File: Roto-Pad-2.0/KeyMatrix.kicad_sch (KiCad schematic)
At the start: 50 parts

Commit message: completed schematic, passes ERC
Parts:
- D1, D10, D11, D12, D13, D14, D15, D16, D17, D18, D19, D2, D20, D21, D22, D23, D24, D25, D3, D4, D5, D6, D7, D8, D9: footprint (none) -> PCM_Diode_SMD_AKL:D_1206_3216Metric_Castellated
- SW1: renamed from S1; value Key -> Switch; footprint (none) -> PCM_Switch_Keyboard_Hotswap_Kailh:SW_Hotswap_Kailh_MX_1.00u; symbol PCM_Elektuur:S-make -> Custom:MX_Keyswitch; Rating V/A -> (none)
- SW10: renamed from S10; value Key -> Switch; footprint (none) -> PCM_Switch_Keyboard_Hotswap_Kailh:SW_Hotswap_Kailh_MX_1.00u; symbol PCM_Elektuur:S-make -> Custom:MX_Keyswitch; Rating V/A -> (none)
- SW11: renamed from S11; value Key -> Switch; footprint (none) -> PCM_Switch_Keyboard_Hotswap_Kailh:SW_Hotswap_Kailh_MX_1.00u; symbol PCM_Elektuur:S-make -> Custom:MX_Keyswitch; Rating V/A -> (none)
- SW12: renamed from S12; value Key -> Switch; footprint (none) -> PCM_Switch_Keyboard_Hotswap_Kailh:SW_Hotswap_Kailh_MX_1.00u; symbol PCM_Elektuur:S-make -> Custom:MX_Keyswitch; Rating V/A -> (none)
- SW13: renamed from S13; value Key -> Switch; footprint (none) -> PCM_Switch_Keyboard_Hotswap_Kailh:SW_Hotswap_Kailh_MX_1.00u; symbol PCM_Elektuur:S-make -> Custom:MX_Keyswitch; Rating V/A -> (none)
- SW14: renamed from S14; value Key -> Switch; footprint (none) -> PCM_Switch_Keyboard_Hotswap_Kailh:SW_Hotswap_Kailh_MX_1.00u; symbol PCM_Elektuur:S-make -> Custom:MX_Keyswitch; Rating V/A -> (none)
- SW15: renamed from S15; value Key -> Switch; footprint (none) -> PCM_Switch_Keyboard_Hotswap_Kailh:SW_Hotswap_Kailh_MX_1.00u; symbol PCM_Elektuur:S-make -> Custom:MX_Keyswitch; Rating V/A -> (none)
- SW16: renamed from S16; value Key -> Switch; footprint (none) -> PCM_Switch_Keyboard_Hotswap_Kailh:SW_Hotswap_Kailh_MX_1.00u; symbol PCM_Elektuur:S-make -> Custom:MX_Keyswitch; Rating V/A -> (none)
- SW17: renamed from S17; value Key -> Switch; footprint (none) -> PCM_Switch_Keyboard_Hotswap_Kailh:SW_Hotswap_Kailh_MX_1.00u; symbol PCM_Elektuur:S-make -> Custom:MX_Keyswitch; Rating V/A -> (none)
- SW18: renamed from S18; value Key -> Switch; footprint (none) -> PCM_Switch_Keyboard_Hotswap_Kailh:SW_Hotswap_Kailh_MX_1.00u; symbol PCM_Elektuur:S-make -> Custom:MX_Keyswitch; Rating V/A -> (none)
- SW19: renamed from S19; value Key -> Switch; footprint (none) -> PCM_Switch_Keyboard_Hotswap_Kailh:SW_Hotswap_Kailh_MX_1.00u; symbol PCM_Elektuur:S-make -> Custom:MX_Keyswitch; Rating V/A -> (none)
- SW2: renamed from S2; value Key -> Switch; footprint (none) -> PCM_Switch_Keyboard_Hotswap_Kailh:SW_Hotswap_Kailh_MX_1.00u; symbol PCM_Elektuur:S-make -> Custom:MX_Keyswitch; Rating V/A -> (none)
- SW20: renamed from S20; value Key -> Switch; footprint (none) -> PCM_Switch_Keyboard_Hotswap_Kailh:SW_Hotswap_Kailh_MX_1.00u; symbol PCM_Elektuur:S-make -> Custom:MX_Keyswitch; Rating V/A -> (none)
- SW21: renamed from S21; value Key -> Switch; footprint (none) -> PCM_Switch_Keyboard_Hotswap_Kailh:SW_Hotswap_Kailh_MX_1.00u; symbol PCM_Elektuur:S-make -> Custom:MX_Keyswitch; Rating V/A -> (none)
- SW22: renamed from S22; value Key -> Switch; footprint (none) -> PCM_Switch_Keyboard_Hotswap_Kailh:SW_Hotswap_Kailh_MX_1.00u; symbol PCM_Elektuur:S-make -> Custom:MX_Keyswitch; Rating V/A -> (none)
- SW23: renamed from S23; value Key -> Switch; footprint (none) -> PCM_Switch_Keyboard_Hotswap_Kailh:SW_Hotswap_Kailh_MX_1.00u; symbol PCM_Elektuur:S-make -> Custom:MX_Keyswitch; Rating V/A -> (none)
- SW24: renamed from S24; value Key -> Switch; footprint (none) -> PCM_Switch_Keyboard_Hotswap_Kailh:SW_Hotswap_Kailh_MX_1.00u; symbol PCM_Elektuur:S-make -> Custom:MX_Keyswitch; Rating V/A -> (none)
- SW25: renamed from S25; value Key -> Switch; footprint (none) -> PCM_Switch_Keyboard_Hotswap_Kailh:SW_Hotswap_Kailh_MX_1.00u; symbol PCM_Elektuur:S-make -> Custom:MX_Keyswitch; Rating V/A -> (none)
- SW3: renamed from S3; value Key -> Switch; footprint (none) -> PCM_Switch_Keyboard_Hotswap_Kailh:SW_Hotswap_Kailh_MX_1.00u; symbol PCM_Elektuur:S-make -> Custom:MX_Keyswitch; Rating V/A -> (none)
- SW4: renamed from S4; value Key -> Switch; footprint (none) -> PCM_Switch_Keyboard_Hotswap_Kailh:SW_Hotswap_Kailh_MX_1.00u; symbol PCM_Elektuur:S-make -> Custom:MX_Keyswitch; Rating V/A -> (none)
- SW5: renamed from S5; value Key -> Switch; footprint (none) -> PCM_Switch_Keyboard_Hotswap_Kailh:SW_Hotswap_Kailh_MX_1.00u; symbol PCM_Elektuur:S-make -> Custom:MX_Keyswitch; Rating V/A -> (none)
- SW6: renamed from S6; value Key -> Switch; footprint (none) -> PCM_Switch_Keyboard_Hotswap_Kailh:SW_Hotswap_Kailh_MX_1.00u; symbol PCM_Elektuur:S-make -> Custom:MX_Keyswitch; Rating V/A -> (none)
- SW7: renamed from S7; value Key -> Switch; footprint (none) -> PCM_Switch_Keyboard_Hotswap_Kailh:SW_Hotswap_Kailh_MX_1.00u; symbol PCM_Elektuur:S-make -> Custom:MX_Keyswitch; Rating V/A -> (none)
- SW8: renamed from S8; value Key -> Switch; footprint (none) -> PCM_Switch_Keyboard_Hotswap_Kailh:SW_Hotswap_Kailh_MX_1.00u; symbol PCM_Elektuur:S-make -> Custom:MX_Keyswitch; Rating V/A -> (none)
- SW9: renamed from S9; value Key -> Switch; footprint (none) -> PCM_Switch_Keyboard_Hotswap_Kailh:SW_Hotswap_Kailh_MX_1.00u; symbol PCM_Elektuur:S-make -> Custom:MX_Keyswitch; Rating V/A -> (none)
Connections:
- net Row 1: now also SW1.1, SW2.1, SW3.1, SW4.1, SW5.1; no longer SW1.4, SW2.4, SW3.4, SW4.4, SW5.4
- net Row 2: now also SW10.1, SW6.1, SW7.1, SW8.1, SW9.1; no longer SW10.4, SW6.4, SW7.4, SW8.4, SW9.4
- net Row 3: now also SW11.1, SW12.1, SW13.1, SW14.1, SW15.1; no longer SW11.4, SW12.4, SW13.4, SW14.4, SW15.4
- net Row 4: now also SW16.1, SW17.1, SW18.1, SW19.1, SW20.1; no longer SW16.4, SW17.4, SW18.4, SW19.4, SW20.4
- net Row 5: now also SW21.1, SW22.1, SW23.1, SW24.1, SW25.1; no longer SW21.4, SW22.4, SW23.4, SW24.4, SW25.4
- net at D11.2 (A+): now also SW11.2; no longer SW11.3
- net at D6.2 (A+): now also SW6.2; no longer SW6.3
- net at D2.2 (A+): now also SW2.2; no longer SW2.3
- net at D18.2 (A+): now also SW18.2; no longer SW18.3
- net at D5.2 (A+): now also SW5.2; no longer SW5.3
- net at D17.2 (A+): now also SW17.2; no longer SW17.3
- net at D20.2 (A+): now also SW20.2; no longer SW20.3
- net at D19.2 (A+): now also SW19.2; no longer SW19.3
- net at D16.2 (A+): now also SW16.2; no longer SW16.3
- net at D12.2 (A+): now also SW12.2; no longer SW12.3
- net at D23.2 (A+): now also SW23.2; no longer SW23.3
- net at D24.2 (A+): now also SW24.2; no longer SW24.3
- net at D9.2 (A+): now also SW9.2; no longer SW9.3
- net at D1.2 (A+): now also SW1.2; no longer SW1.3
- net at D21.2 (A+): now also SW21.2; no longer SW21.3
- net at D15.2 (A+): now also SW15.2; no longer SW15.3
- net at D8.2 (A+): now also SW8.2; no longer SW8.3
- net at D4.2 (A+): now also SW4.2; no longer SW4.3
- net at D7.2 (A+): now also SW7.2; no longer SW7.3
- net at D10.2 (A+): now also SW10.2; no longer SW10.3
- net at D22.2 (A+): now also SW22.2; no longer SW22.3
- net at D25.2 (A+): now also SW25.2; no longer SW25.3
- net at D14.2 (A+): now also SW14.2; no longer SW14.3
- net at D3.2 (A+): now also SW3.2; no longer SW3.3
- net at D13.2 (A+): now also SW13.2; no longer SW13.3

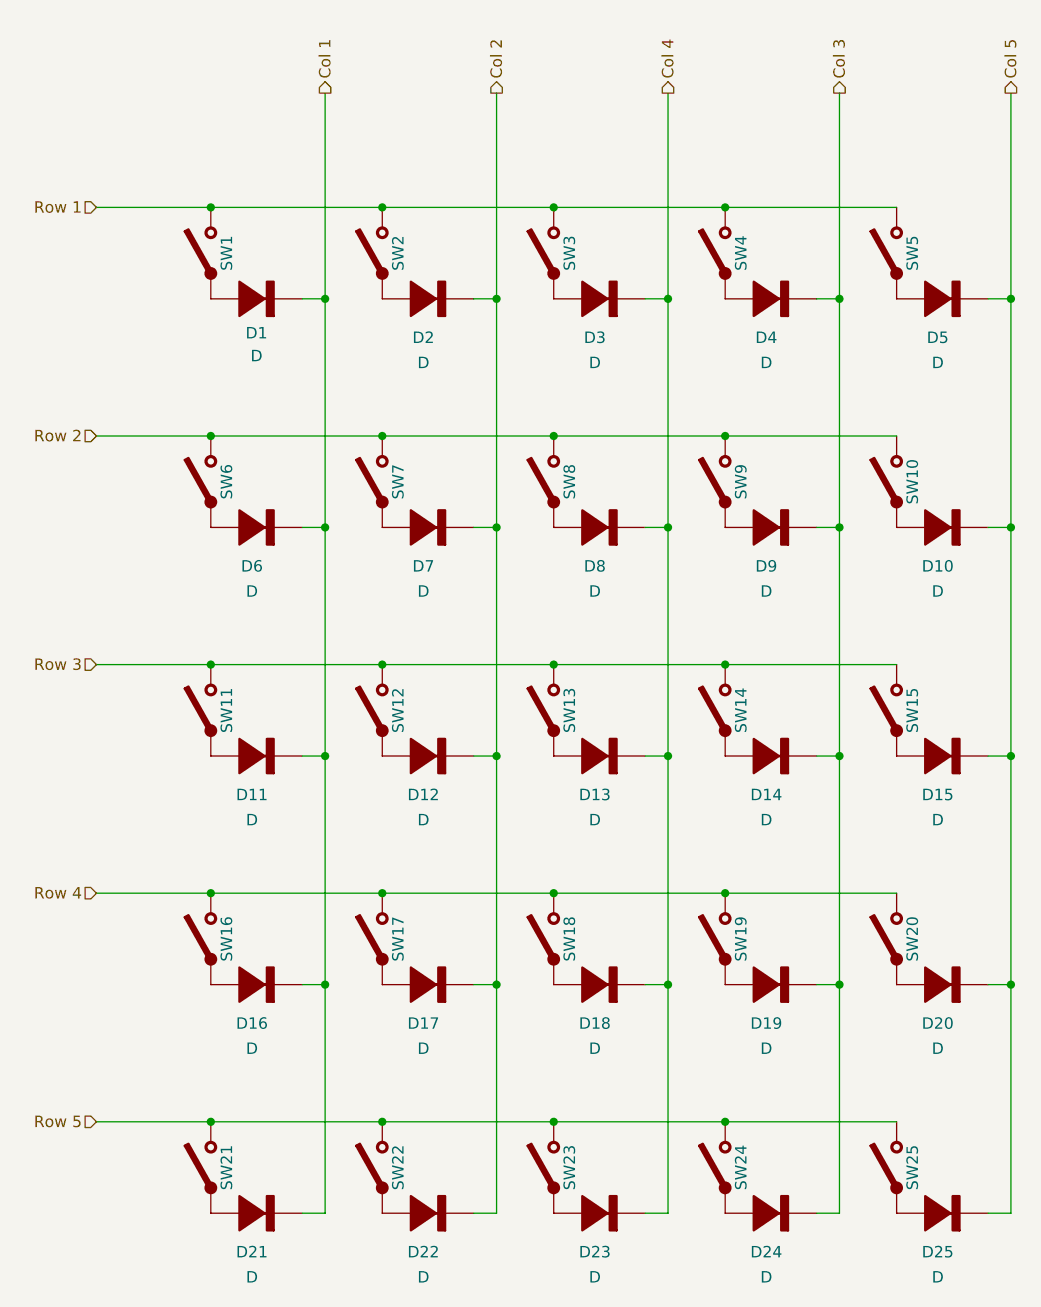
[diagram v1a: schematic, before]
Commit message: added more heirarchical sheets, debouncing
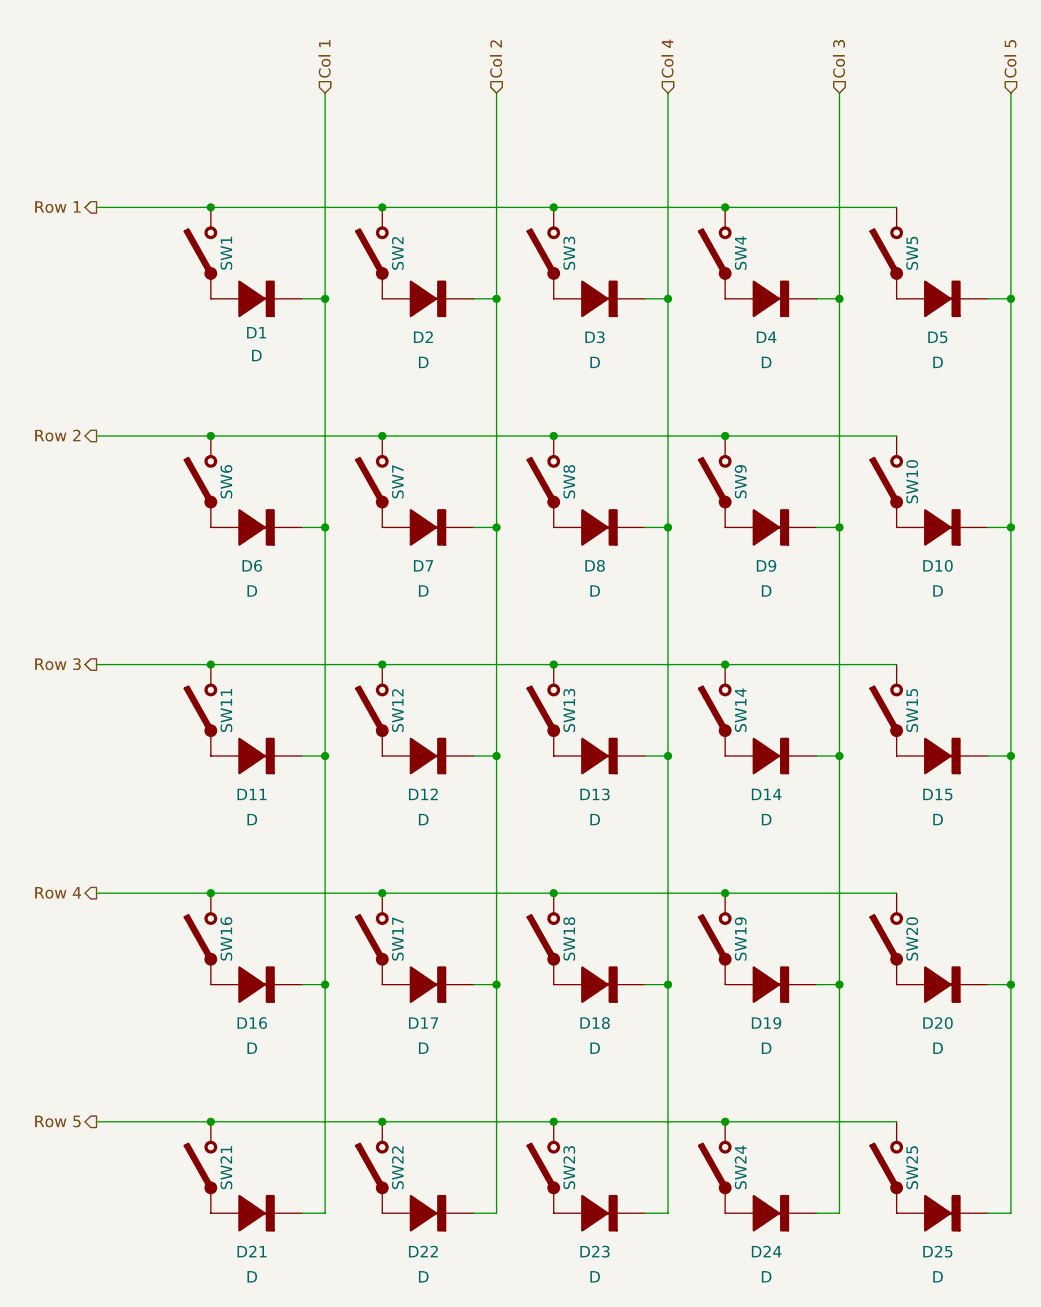
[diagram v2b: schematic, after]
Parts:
- D1, D10, D11, D12, D13, D14, D15, D16, D17, D18, D19, D2, D20, D21, D22, D23, D24, D25, D3, D4, D5, D6, D7, D8, D9: footprint PCM_Diode_SMD_AKL:D_1206_3216Metric_Castellated -> Keebio-Parts.pretty-master:Diode-dual
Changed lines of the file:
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@@
 	)
 	(hierarchical_label "Col 4"
-		(shape output)
+		(shape input)
 		(at 114.3 25.4 90)
 		(effects
@@
 	)
 	(hierarchical_label "Col 3"
-		(shape output)
+		(shape input)
 		(at 133.35 25.4 90)
 		(effects
@@
 	)
 	(hierarchical_label "Col 2"
-		(shape output)
+		(shape input)
 		(at 95.25 25.4 90)
 		(effects
@@
 	)
 	(hierarchical_label "Row 3"
-		(shape input)
+		(shape output)
 		(at 50.8 88.9 180)
 		(effects
@@
 	)
 	(hierarchical_label "Row 2"
-		(shape input)
+		(shape output)
 		(at 50.8 63.5 180)
 		(effects
@@
 	)
 	(hierarchical_label "Row 1"
-		(shape input)
+		(shape output)
 		(at 50.8 38.1 180)
 		(effects
@@
 	)
 	(hierarchical_label "Row 5"
-		(shape input)
+		(shape output)
 		(at 50.8 139.7 180)
 		(effects
@@
 	)
 	(hierarchical_label "Row 4"
-		(shape input)
+		(shape output)
 		(at 50.8 114.3 180)
 		(effects
@@
 	)
 	(hierarchical_label "Col 1"
-		(shape output)
+		(shape input)
 		(at 76.2 25.4 90)
 		(effects
@@
 	)
 	(hierarchical_label "Col 5"
-		(shape output)
+		(shape input)
 		(at 152.4 25.4 90)
 		(effects
@@
 			)
 		)
-		(property "Footprint" "PCM_Diode_SMD_AKL:D_1206_3216Metric_Castellated"
+		(property "Footprint" "Keebio-Parts.pretty-master:Diode-dual"
 			(at 87.63 48.26 0)
 			(effects
@@
 			)
 		)
-		(property "Footprint" "PCM_Diode_SMD_AKL:D_1206_3216Metric_Castellated"
+		(property "Footprint" "Keebio-Parts.pretty-master:Diode-dual"
 			(at 144.78 48.26 0)
 			(effects
@@
 			)
 		)
-		(property "Footprint" "PCM_Diode_SMD_AKL:D_1206_3216Metric_Castellated"
+		(property "Footprint" "Keebio-Parts.pretty-master:Diode-dual"
 			(at 144.78 124.46 0)
 			(effects
@@
 			)
 		)
-		(property "Footprint" "PCM_Diode_SMD_AKL:D_1206_3216Metric_Castellated"
+		(property "Footprint" "Keebio-Parts.pretty-master:Diode-dual"
 			(at 125.73 124.46 0)
 			(effects
@@
 			)
 		)
-		(property "Footprint" "PCM_Diode_SMD_AKL:D_1206_3216Metric_Castellated"
+		(property "Footprint" "Keebio-Parts.pretty-master:Diode-dual"
 			(at 68.58 124.46 0)
 			(effects
@@
 			)
 		)
-		(property "Footprint" "PCM_Diode_SMD_AKL:D_1206_3216Metric_Castellated"
+		(property "Footprint" "Keebio-Parts.pretty-master:Diode-dual"
 			(at 87.63 99.06 0)
 			(effects
@@
 			)
 		)
-		(property "Footprint" "PCM_Diode_SMD_AKL:D_1206_3216Metric_Castellated"
+		(property "Footprint" "Keebio-Parts.pretty-master:Diode-dual"
 			(at 106.68 73.66 0)
 			(effects
@@
 			)
 		)
-		(property "Footprint" "PCM_Diode_SMD_AKL:D_1206_3216Metric_Castellated"
+		(property "Footprint" "Keebio-Parts.pretty-master:Diode-dual"
 			(at 125.73 48.26 0)
 			(effects
@@
 			)
 		)
-		(property "Footprint" "PCM_Diode_SMD_AKL:D_1206_3216Metric_Castellated"
+		(property "Footprint" "Keebio-Parts.pretty-master:Diode-dual"
 			(at 125.73 73.66 0)
 			(effects
@@
 			)
 		)
-		(property "Footprint" "PCM_Diode_SMD_AKL:D_1206_3216Metric_Castellated"
+		(property "Footprint" "Keebio-Parts.pretty-master:Diode-dual"
 			(at 144.78 73.66 0)
 			(effects
@@
 			)
 		)
-		(property "Footprint" "PCM_Diode_SMD_AKL:D_1206_3216Metric_Castellated"
+		(property "Footprint" "Keebio-Parts.pretty-master:Diode-dual"
 			(at 87.63 149.86 0)
 			(effects
@@
 			)
 		)
-		(property "Footprint" "PCM_Diode_SMD_AKL:D_1206_3216Metric_Castellated"
+		(property "Footprint" "Keebio-Parts.pretty-master:Diode-dual"
 			(at 68.58 149.86 0)
 			(effects
@@
 			)
 		)
-		(property "Footprint" "PCM_Diode_SMD_AKL:D_1206_3216Metric_Castellated"
+		(property "Footprint" "Keebio-Parts.pretty-master:Diode-dual"
 			(at 144.78 149.86 0)
 			(effects
@@
 			)
 		)
-		(property "Footprint" "PCM_Diode_SMD_AKL:D_1206_3216Metric_Castellated"
+		(property "Footprint" "Keebio-Parts.pretty-master:Diode-dual"
 			(at 144.78 99.06 0)
 			(effects
@@
 			)
 		)
-		(property "Footprint" "PCM_Diode_SMD_AKL:D_1206_3216Metric_Castellated"
+		(property "Footprint" "Keebio-Parts.pretty-master:Diode-dual"
 			(at 68.58 99.06 0)
 			(effects
@@
 			)
 		)
-		(property "Footprint" "PCM_Diode_SMD_AKL:D_1206_3216Metric_Castellated"
+		(property "Footprint" "Keebio-Parts.pretty-master:Diode-dual"
 			(at 68.58 48.26 0)
 			(effects
@@
 			)
 		)
-		(property "Footprint" "PCM_Diode_SMD_AKL:D_1206_3216Metric_Castellated"
+		(property "Footprint" "Keebio-Parts.pretty-master:Diode-dual"
 			(at 106.68 149.86 0)
 			(effects
@@
 			)
 		)
-		(property "Footprint" "PCM_Diode_SMD_AKL:D_1206_3216Metric_Castellated"
+		(property "Footprint" "Keebio-Parts.pretty-master:Diode-dual"
 			(at 68.58 73.66 0)
 			(effects
@@
 			)
 		)
-		(property "Footprint" "PCM_Diode_SMD_AKL:D_1206_3216Metric_Castellated"
+		(property "Footprint" "Keebio-Parts.pretty-master:Diode-dual"
 			(at 106.68 99.06 0)
 			(effects
@@
 			)
 		)
-		(property "Footprint" "PCM_Diode_SMD_AKL:D_1206_3216Metric_Castellated"
+		(property "Footprint" "Keebio-Parts.pretty-master:Diode-dual"
 			(at 125.73 99.06 0)
 			(effects
@@
 			)
 		)
-		(property "Footprint" "PCM_Diode_SMD_AKL:D_1206_3216Metric_Castellated"
+		(property "Footprint" "Keebio-Parts.pretty-master:Diode-dual"
 			(at 125.73 149.86 0)
 			(effects
@@
 			)
 		)
-		(property "Footprint" "PCM_Diode_SMD_AKL:D_1206_3216Metric_Castellated"
+		(property "Footprint" "Keebio-Parts.pretty-master:Diode-dual"
 			(at 87.63 124.46 0)
 			(effects
@@
 			)
 		)
-		(property "Footprint" "PCM_Diode_SMD_AKL:D_1206_3216Metric_Castellated"
+		(property "Footprint" "Keebio-Parts.pretty-master:Diode-dual"
 			(at 106.68 124.46 0)
 			(effects
@@
 			)
 		)
-		(property "Footprint" "PCM_Diode_SMD_AKL:D_1206_3216Metric_Castellated"
+		(property "Footprint" "Keebio-Parts.pretty-master:Diode-dual"
 			(at 106.68 48.26 0)
 			(effects
@@
 			)
 		)
-		(property "Footprint" "PCM_Diode_SMD_AKL:D_1206_3216Metric_Castellated"
+		(property "Footprint" "Keebio-Parts.pretty-master:Diode-dual"
 			(at 87.63 73.66 0)
 			(effects

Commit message: layout completed, first draft of routing
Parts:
- D1, D10, D11, D12, D13, D14, D15, D16, D17, D18, D19, D2, D20, D21, D22, D23, D24, D25, D3, D4, D5, D6, D7, D8, D9: footprint Keebio-Parts.pretty-master:Diode-dual -> PCM_Diode_SMD_AKL:D_SMA
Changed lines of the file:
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@@
 			)
 		)
-		(property "Footprint" "Keebio-Parts.pretty-master:Diode-dual"
+		(property "Footprint" "PCM_Diode_SMD_AKL:D_SMA"
 			(at 87.63 48.26 0)
 			(effects
@@
 			)
 		)
-		(property "Footprint" "Keebio-Parts.pretty-master:Diode-dual"
+		(property "Footprint" "PCM_Diode_SMD_AKL:D_SMA"
 			(at 144.78 48.26 0)
 			(effects
@@
 			)
 		)
-		(property "Footprint" "Keebio-Parts.pretty-master:Diode-dual"
+		(property "Footprint" "PCM_Diode_SMD_AKL:D_SMA"
 			(at 144.78 124.46 0)
 			(effects
@@
 			)
 		)
-		(property "Footprint" "Keebio-Parts.pretty-master:Diode-dual"
+		(property "Footprint" "PCM_Diode_SMD_AKL:D_SMA"
 			(at 125.73 124.46 0)
 			(effects
@@
 			)
 		)
-		(property "Footprint" "Keebio-Parts.pretty-master:Diode-dual"
+		(property "Footprint" "PCM_Diode_SMD_AKL:D_SMA"
 			(at 68.58 124.46 0)
 			(effects
@@
 			)
 		)
-		(property "Footprint" "Keebio-Parts.pretty-master:Diode-dual"
+		(property "Footprint" "PCM_Diode_SMD_AKL:D_SMA"
 			(at 87.63 99.06 0)
 			(effects
@@
 			)
 		)
-		(property "Footprint" "Keebio-Parts.pretty-master:Diode-dual"
+		(property "Footprint" "PCM_Diode_SMD_AKL:D_SMA"
 			(at 106.68 73.66 0)
 			(effects
@@
 			)
 		)
-		(property "Footprint" "Keebio-Parts.pretty-master:Diode-dual"
+		(property "Footprint" "PCM_Diode_SMD_AKL:D_SMA"
 			(at 125.73 48.26 0)
 			(effects
@@
 			)
 		)
-		(property "Footprint" "Keebio-Parts.pretty-master:Diode-dual"
+		(property "Footprint" "PCM_Diode_SMD_AKL:D_SMA"
 			(at 125.73 73.66 0)
 			(effects
@@
 			)
 		)
-		(property "Footprint" "Keebio-Parts.pretty-master:Diode-dual"
+		(property "Footprint" "PCM_Diode_SMD_AKL:D_SMA"
 			(at 144.78 73.66 0)
 			(effects
@@
 			)
 		)
-		(property "Footprint" "Keebio-Parts.pretty-master:Diode-dual"
+		(property "Footprint" "PCM_Diode_SMD_AKL:D_SMA"
 			(at 87.63 149.86 0)
 			(effects
@@
 			)
 		)
-		(property "Footprint" "Keebio-Parts.pretty-master:Diode-dual"
+		(property "Footprint" "PCM_Diode_SMD_AKL:D_SMA"
 			(at 68.58 149.86 0)
 			(effects
@@
 			)
 		)
-		(property "Footprint" "Keebio-Parts.pretty-master:Diode-dual"
+		(property "Footprint" "PCM_Diode_SMD_AKL:D_SMA"
 			(at 144.78 149.86 0)
 			(effects
@@
 			)
 		)
-		(property "Footprint" "Keebio-Parts.pretty-master:Diode-dual"
+		(property "Footprint" "PCM_Diode_SMD_AKL:D_SMA"
 			(at 144.78 99.06 0)
 			(effects
@@
 			)
 		)
-		(property "Footprint" "Keebio-Parts.pretty-master:Diode-dual"
+		(property "Footprint" "PCM_Diode_SMD_AKL:D_SMA"
 			(at 68.58 99.06 0)
 			(effects
@@
 			)
 		)
-		(property "Footprint" "Keebio-Parts.pretty-master:Diode-dual"
+		(property "Footprint" "PCM_Diode_SMD_AKL:D_SMA"
 			(at 68.58 48.26 0)
 			(effects
@@
 			)
 		)
-		(property "Footprint" "Keebio-Parts.pretty-master:Diode-dual"
+		(property "Footprint" "PCM_Diode_SMD_AKL:D_SMA"
 			(at 106.68 149.86 0)
 			(effects
@@
 			)
 		)
-		(property "Footprint" "Keebio-Parts.pretty-master:Diode-dual"
+		(property "Footprint" "PCM_Diode_SMD_AKL:D_SMA"
 			(at 68.58 73.66 0)
 			(effects
@@
 			)
 		)
-		(property "Footprint" "Keebio-Parts.pretty-master:Diode-dual"
+		(property "Footprint" "PCM_Diode_SMD_AKL:D_SMA"
 			(at 106.68 99.06 0)
 			(effects
@@
 			)
 		)
-		(property "Footprint" "Keebio-Parts.pretty-master:Diode-dual"
+		(property "Footprint" "PCM_Diode_SMD_AKL:D_SMA"
 			(at 125.73 99.06 0)
 			(effects
@@
 			)
 		)
-		(property "Footprint" "Keebio-Parts.pretty-master:Diode-dual"
+		(property "Footprint" "PCM_Diode_SMD_AKL:D_SMA"
 			(at 125.73 149.86 0)
 			(effects
@@
 			)
 		)
-		(property "Footprint" "Keebio-Parts.pretty-master:Diode-dual"
+		(property "Footprint" "PCM_Diode_SMD_AKL:D_SMA"
 			(at 87.63 124.46 0)
 			(effects
@@
 			)
 		)
-		(property "Footprint" "Keebio-Parts.pretty-master:Diode-dual"
+		(property "Footprint" "PCM_Diode_SMD_AKL:D_SMA"
 			(at 106.68 124.46 0)
 			(effects
@@
 			)
 		)
-		(property "Footprint" "Keebio-Parts.pretty-master:Diode-dual"
+		(property "Footprint" "PCM_Diode_SMD_AKL:D_SMA"
 			(at 106.68 48.26 0)
 			(effects
@@
 			)
 		)
-		(property "Footprint" "Keebio-Parts.pretty-master:Diode-dual"
+		(property "Footprint" "PCM_Diode_SMD_AKL:D_SMA"
 			(at 87.63 73.66 0)
 			(effects
